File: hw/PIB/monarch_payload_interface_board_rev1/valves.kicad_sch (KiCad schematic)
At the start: 4 parts, among them U3 NZT7053

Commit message: More components
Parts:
- removed D1: 1SMA4757, Zener_diode:DIOM4325X250N, symbol 1SMA4757:1SMA4757
- removed R1: RMCF1206JT330R, 330O res:STA_RMCF1206_STP-L, symbol 330O res:RMCF1206JT330R
- removed U3: NZT7053, nzt7:SOT-223_ONS-L, symbol nzt7:NZT7053
- added CR10, CR11, CR12, CR13, CR14, CR15, CR16, CR17, CR18, CR2, CR3, CR4, CR5, CR6, CR7, CR8, CR9: S1J-13-F, s1j:SMA_DIO-L, symbol s1j:S1J-13-F
- added Q1, Q10, Q11, Q12, Q13, Q14, Q15, Q16, Q17, Q18, Q2, Q3, Q4, Q5, Q6, Q7, Q8, Q9: FZT600TA, fzt:SOT230P700X170-4N, symbol FZT600TA:FZT600TA
- added R1, R10, R11, R12, R13, R14, R15, R16, R2, R3, R30, R31, R4, R5, R6, R7, R8, R9: 125, Resistor_SMD:R_0402_1005Metric, symbol Device:R_Small
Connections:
- net 12VA: now reaches CR1.1
- net 12VA: now also CR10.1, CR11.1, CR12.1, CR13.1, CR14.1, CR15.1, CR16.1, CR17.1, CR18.1, CR2.1, CR3.1, CR5.1, CR7.1, CR8.1, CR9.1
- net Valve1-: now reaches CR1.2
- net Valve1-: now also Q1.2 (C_1), Q1.4 (C_2)
- new net: Q3.1 (B), R3.2
- new net: Q6.1 (B), R6.2
- new net: Q5.1 (B), R5.2
- new net: Q15.1 (B), R15.2
- new net: Q8.1 (B), R8.2
- new net: Q12.1 (B), R12.2
- new net: Q7.1 (B), R7.2
- new net: Q13.1 (B), R13.2
- new net: Q14.1 (B), R14.2
- new net: Q4.1 (B), R4.2
- new net: Q17.1 (B), R30.2
- new net: Q16.1 (B), R16.2
- new net: Q2.1 (B), R2.2
- new net: Q10.1 (B), R10.2
- new net: Q1.1 (B), R1.2
- new net: Q18.1 (B), R31.2
- new net: Q9.1 (B), R9.2
- new net: Q11.1 (B), R11.2
- new net 12VB: CR4.1, CR6.1
- new net GND: Q1.3 (E), Q10.3 (E), Q11.3 (E), Q12.3 (E), Q13.3 (E), Q14.3 (E), Q15.3 (E), Q16.3 (E), Q17.3 (E), Q18.3 (E), Q2.3 (E), Q3.3 (E), Q4.3 (E), Q5.3 (E), Q6.3 (E), Q7.3 (E), Q8.3 (E), Q9.3 (E)
- new net Valve1: R1.1
- new net Valve10: R10.1
- new net Valve10-: CR10.2, Q10.2 (C_1), Q10.4 (C_2)
- new net Valve11: R11.1
- new net Valve11-: CR11.2, Q11.2 (C_1), Q11.4 (C_2)
- new net Valve12: R12.1
- new net Valve12-: CR12.2, Q12.2 (C_1), Q12.4 (C_2)
- new net Valve13: R13.1
- new net Valve13-: CR13.2, Q13.2 (C_1), Q13.4 (C_2)
- new net Valve14: R14.1
- new net Valve14-: CR14.2, Q14.2 (C_1), Q14.4 (C_2)
- new net Valve15: R15.1
- new net Valve15-: CR15.2, Q15.2 (C_1), Q15.4 (C_2)
- new net Valve16: R16.1
- new net Valve16-: CR16.2, Q16.2 (C_1), Q16.4 (C_2)
- new net Valve17: R30.1
- new net Valve17-: CR17.2, Q17.2 (C_1), Q17.4 (C_2)
- new net Valve18: R31.1
- new net Valve18-: CR18.2, Q18.2 (C_1), Q18.4 (C_2)
- new net Valve2: R2.1
- new net Valve2-: CR2.2, Q2.2 (C_1), Q2.4 (C_2)
- new net Valve3: R3.1
- new net Valve3-: CR3.2, Q3.2 (C_1), Q3.4 (C_2)
- new net Valve4: R4.1
- new net Valve4-: CR4.2, Q4.2 (C_1), Q4.4 (C_2)
- new net Valve5: R5.1
- new net Valve5-: CR5.2, Q5.2 (C_1), Q5.4 (C_2)
- new net Valve6: R6.1
- new net Valve6-: CR6.2, Q6.2 (C_1), Q6.4 (C_2)
- new net Valve7: R7.1
- new net Valve7-: CR7.2, Q7.2 (C_1), Q7.4 (C_2)
- new net Valve8: R8.1
- new net Valve8-: CR8.2, Q8.2 (C_1), Q8.4 (C_2)
- new net Valve9: R9.1
- new net Valve9-: CR9.2, Q9.2 (C_1), Q9.4 (C_2)
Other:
- moved on the sheet: CR1

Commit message: Schematic Review
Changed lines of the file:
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@@
 	)
 	(hierarchical_label "Valve16+"
-		(shape input)
+		(shape output)
 		(at 62.23 153.67 0)
 		(effects
@@
 	)
 	(hierarchical_label "Valve11+"
-		(shape input)
+		(shape output)
 		(at 62.23 111.76 0)
 		(effects
@@
 	)
 	(hierarchical_label "Valve2+"
-		(shape input)
+		(shape output)
 		(at 112.268 27.94 0)
 		(effects
@@
 	)
 	(hierarchical_label "Valve14+"
-		(shape input)
+		(shape output)
 		(at 212.344 111.76 0)
 		(effects
@@
 	)
 	(hierarchical_label "Valve18+"
-		(shape input)
+		(shape output)
 		(at 162.306 153.67 0)
 		(effects
@@
 	)
 	(hierarchical_label "Valve15+"
-		(shape input)
+		(shape output)
 		(at 262.382 111.76 0)
 		(effects
@@
 	)
 	(hierarchical_label "Valve7+"
-		(shape input)
+		(shape output)
 		(at 112.268 69.85 0)
 		(effects
@@
 	)
 	(hierarchical_label "Valve9+"
-		(shape input)
+		(shape output)
 		(at 212.344 69.85 0)
 		(effects
@@
 	)
 	(hierarchical_label "Valve13+"
-		(shape input)
+		(shape output)
 		(at 162.306 111.76 0)
 		(effects
@@
 	)
 	(hierarchical_label "Valve6+"
-		(shape input)
+		(shape output)
 		(at 62.23 69.85 0)
 		(effects
@@
 	)
 	(hierarchical_label "Valve5+"
-		(shape input)
+		(shape output)
 		(at 262.382 27.94 0)
 		(effects
@@
 	)
 	(hierarchical_label "Valve3+"
-		(shape input)
+		(shape output)
 		(at 162.306 27.94 0)
 		(effects
@@
 	)
 	(hierarchical_label "Valve17+"
-		(shape input)
+		(shape output)
 		(at 112.268 153.67 0)
 		(effects
@@
 	)
 	(hierarchical_label "Valve12+"
-		(shape input)
+		(shape output)
 		(at 112.268 111.76 0)
 		(effects
@@
 	)
 	(hierarchical_label "Valve8+"
-		(shape input)
+		(shape output)
 		(at 162.306 69.85 0)
 		(effects
@@
 	)
 	(hierarchical_label "Valve10+"
-		(shape input)
+		(shape output)
 		(at 262.382 69.85 0)
 		(effects
@@
 	)
 	(hierarchical_label "Valve4+"
-		(shape input)
+		(shape output)
 		(at 212.344 27.94 0)
 		(effects
@@
 	)
 	(hierarchical_label "Valve1+"
-		(shape input)
+		(shape output)
 		(at 62.23 27.94 0)
 		(effects

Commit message: PCB updates
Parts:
- R1, R10, R11, R12, R13, R14, R15, R16, R2, R3, R30, R31, R4, R5, R6, R7, R8, R9: footprint Resistor_SMD:R_0402_1005Metric -> Resistor_SMD:R_0603_1608Metric
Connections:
- net 12VA renamed +12VA
- net 12VB renamed +12VB

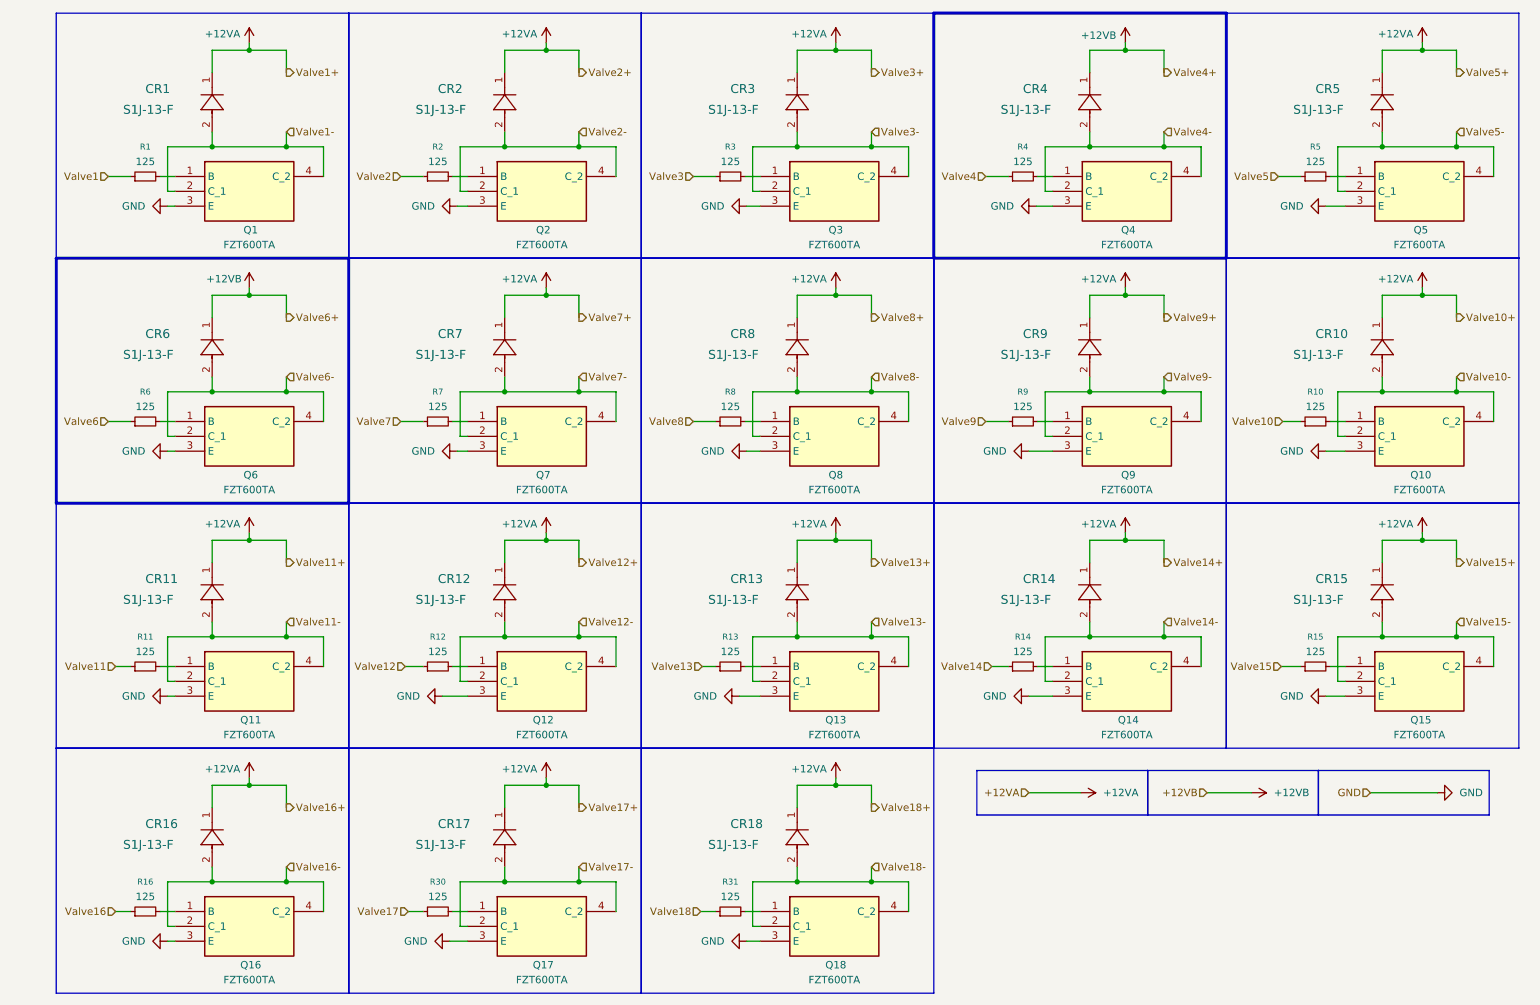
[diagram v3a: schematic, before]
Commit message: PIB layout update
done pending Ben O approval
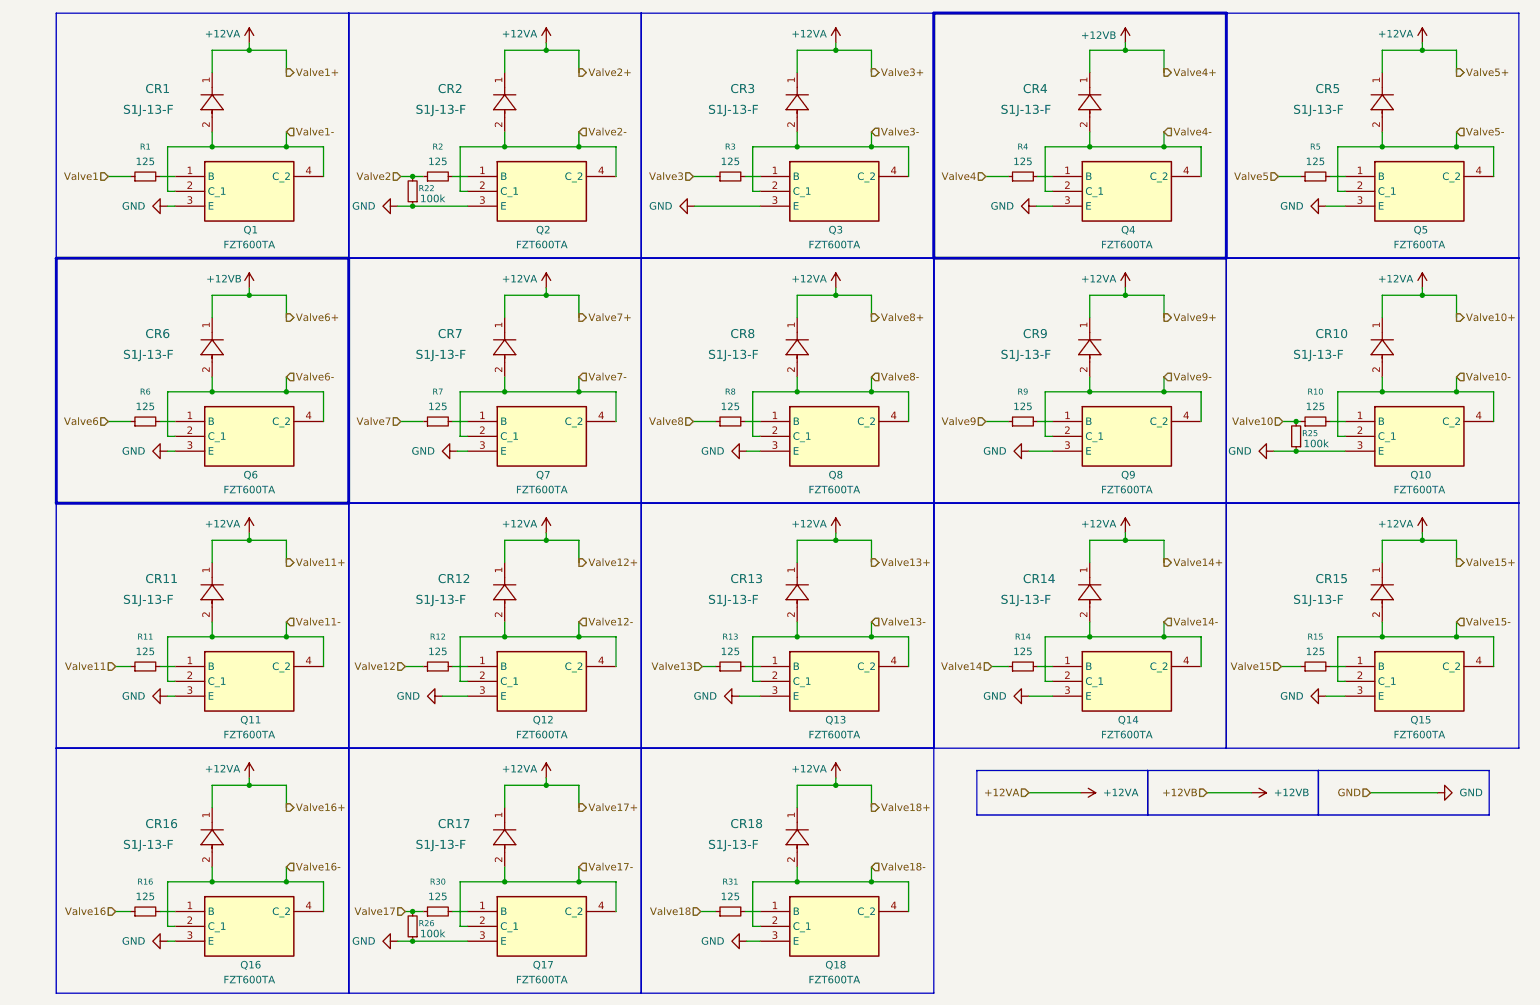
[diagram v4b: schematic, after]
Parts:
- added R22, R25, R26: 100k, Resistor_SMD:R_0603_1608Metric, symbol Device:R_Small
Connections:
- net GND: now also R22.1, R25.1, R26.1
- net Valve10: now also R25.2
- net Valve17: now also R26.2
- net Valve2: now also R22.2
